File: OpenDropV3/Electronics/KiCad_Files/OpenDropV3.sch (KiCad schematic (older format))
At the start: 269 parts, among them J1 USB_C_Receptacle, J2 Conn_02x05_Odd_Even, P1 CONN_01X01, P10 CONN_01X01, P11 CONN_01X01, P12 CONN_01X01, P13 ScrewPad1, P14 ScrewPad2, P15 ScrewPad3, P16 ScrewPad4, P2 ScrewPad4, P3 CONN_01X01, P4 CONN_PSEUDO_AC, P7 CONN_01X01, P8 CONN_01X01, P9 CONN_01X01, SW1 SW_PUSH, SW2 SW_PUSH, SW3 SW_PUSH, SW5 SPST, T1 TK560P60Y, U1 MAX1771ESA, U10 AQY210EH, U11 AQY210EH, U12 AQY210EH, U13 AQY210EH, U14 TLV1117-33, U15 MCP41010, U16 74xx14, U2 HV507, U3 PAM8301, U4 HV507, U5 SAMD21G18B-A changed from SAM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, U6 MCP6002, U7 HCPL0534, U8 HCPL0534, U9 HCPL0534, Y1 32.765

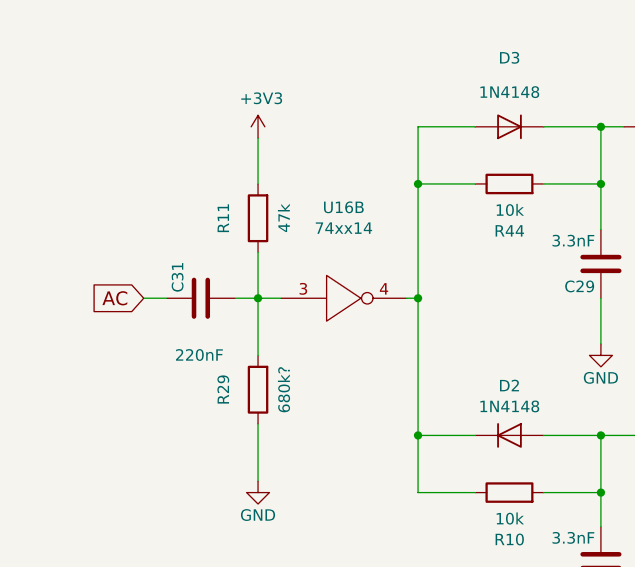
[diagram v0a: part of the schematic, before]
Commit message: Updated to V32 new marked with (new)
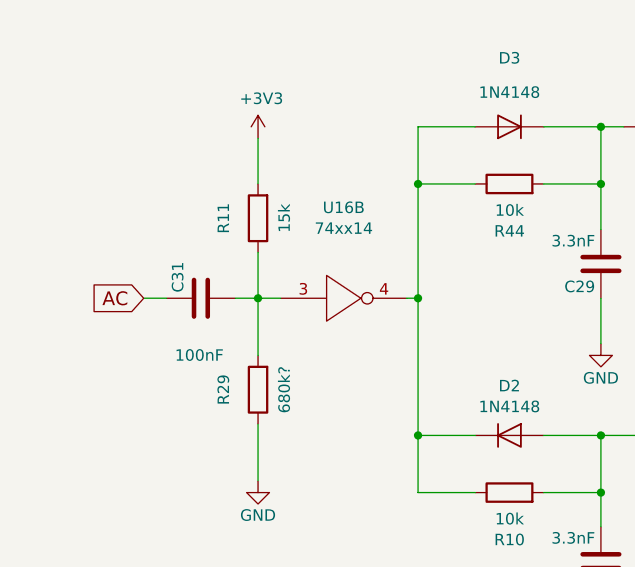
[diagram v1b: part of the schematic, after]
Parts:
- C31: value 220nF -> 100nF
- R11: value 47k -> 15k
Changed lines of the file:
@@
 P 1250 2500
 F 0 "C31" H 1275 2600 50  0000 L CNN
-F 1 "220nF" V 1000 2400 50  0000 L CNN
+F 1 "100nF" V 1000 2400 50  0000 L CNN
 F 2 "Capacitors_SMD:C_0805" H 1288 2350 30  0001 C CNN
 F 3 "" H 1250 2500 60  0000 C CNN
@@
 P 1500 2150
 F 0 "R11" V 1650 2150 50  0000 C CNN
-F 1 "47k" V 1384 2150 50  0000 C CNN
+F 1 "15k" V 1384 2150 50  0000 C CNN
 F 2 "Resistors_SMD:R_0805" V 1430 2150 50  0001 C CNN
 F 3 "" H 1500 2150 50  0001 C CNN
